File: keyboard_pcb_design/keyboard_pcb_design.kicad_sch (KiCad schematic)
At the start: 39 parts, among them J1 USB_C_Receptacle_USB2.0_14P, SW1 Switch, SW2 Switch, SW3 Switch, SW4 Switch, SW5 Switch, U1 SC09147, U2 NCP1117-3.3_SOT223, U3 MX25L3233FM2I-08Q, U4 SMF05CT1G, X1 ABM8-272-T3

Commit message: saved changes
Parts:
- removed J1: USB_C_Receptacle_USB2.0_14P, symbol Connector:USB_C_Receptacle_USB2.0_14P
- added J2: USB4105-GF-A, keyboard_footprint:USB4105_GCT, symbol keyboard_library:USB4105-GF-A
- U4: footprint (none) -> keyboard_footprint:SOT65P210X110-6N
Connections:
- net +5V is gone; now on net +3V3: C1.1, U2.3 (VI), U4.4
- net +3V3: now also J2.A4-B9 (VBUS), J2.B4-A9 (VBUS)
- net GND: now also J2.A1-B12 (GND), J2.B1-A12 (GND)
- net USB_D+: now also J2.A6 (DP1), J2.B6 (DP2)
- net USB_D-: now also J2.A7 (DN1), J2.B7 (DN2)
- net at R1.2: now also J2.A5 (CC1)
- net at R2.2: now also J2.B5 (CC2)
- no-connect marks 1 -> 3
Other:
- moved on the sheet: C1, C2, R1, R2, U2

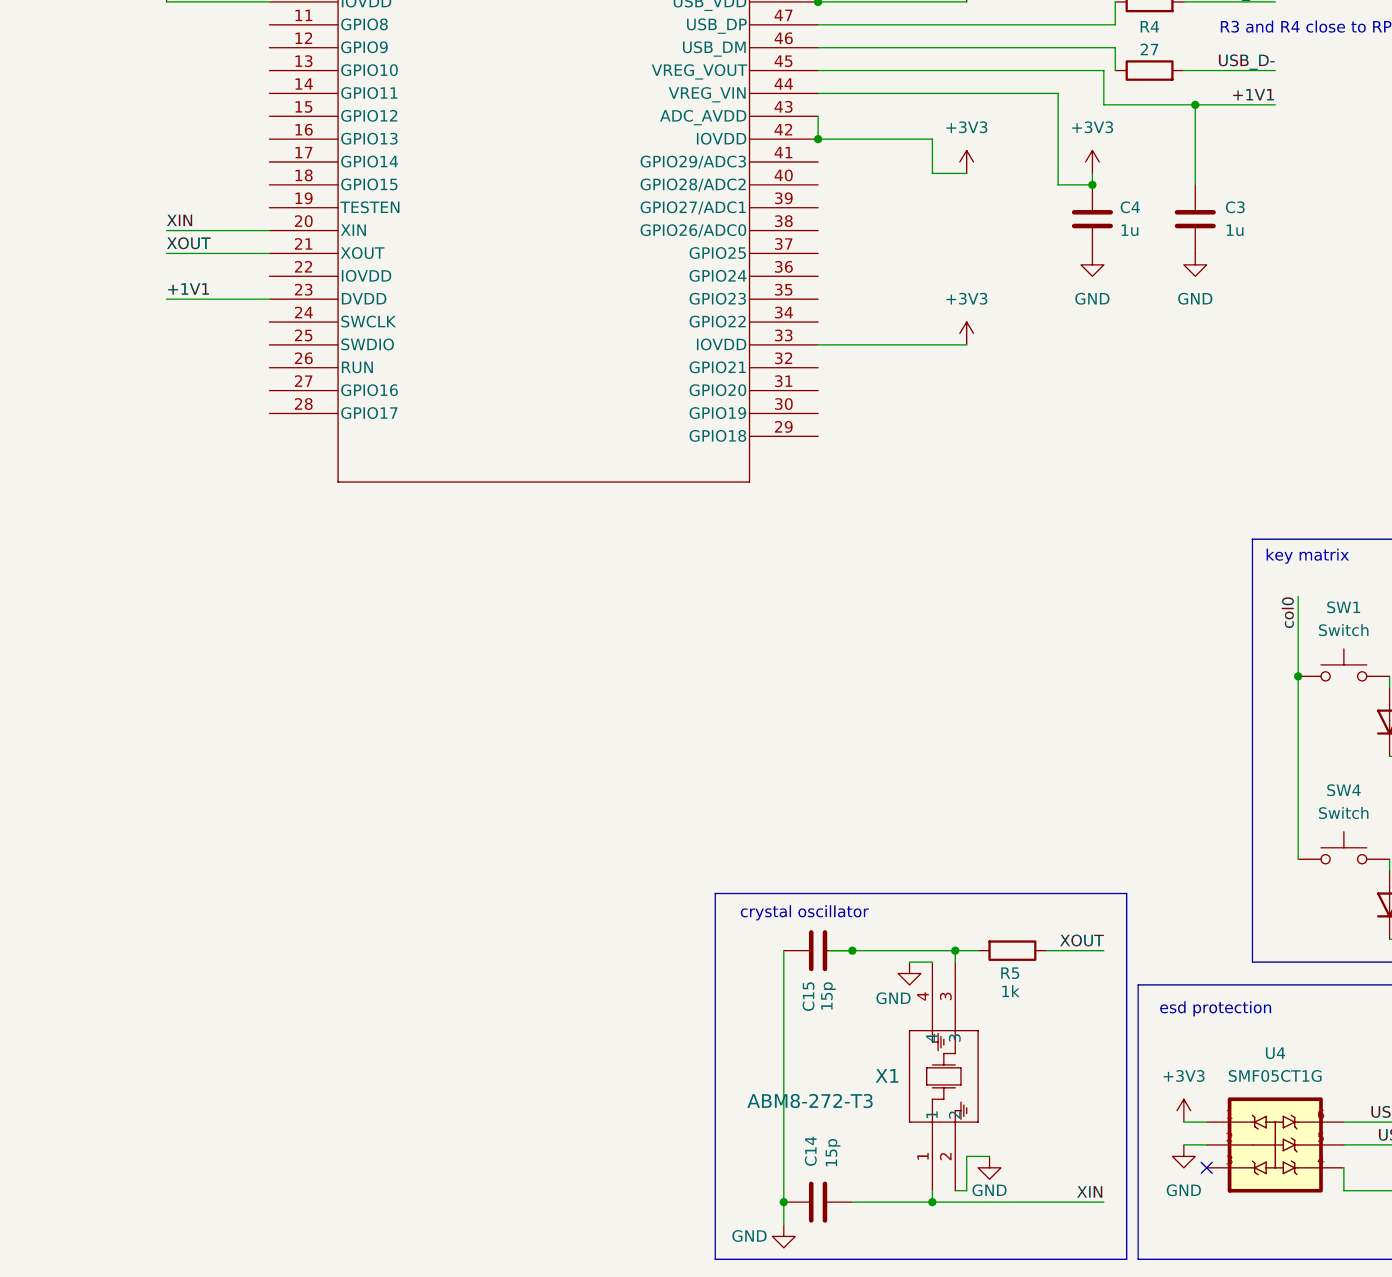
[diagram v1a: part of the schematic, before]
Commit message: update schematic for to usbc 16p and reset/boot buttons
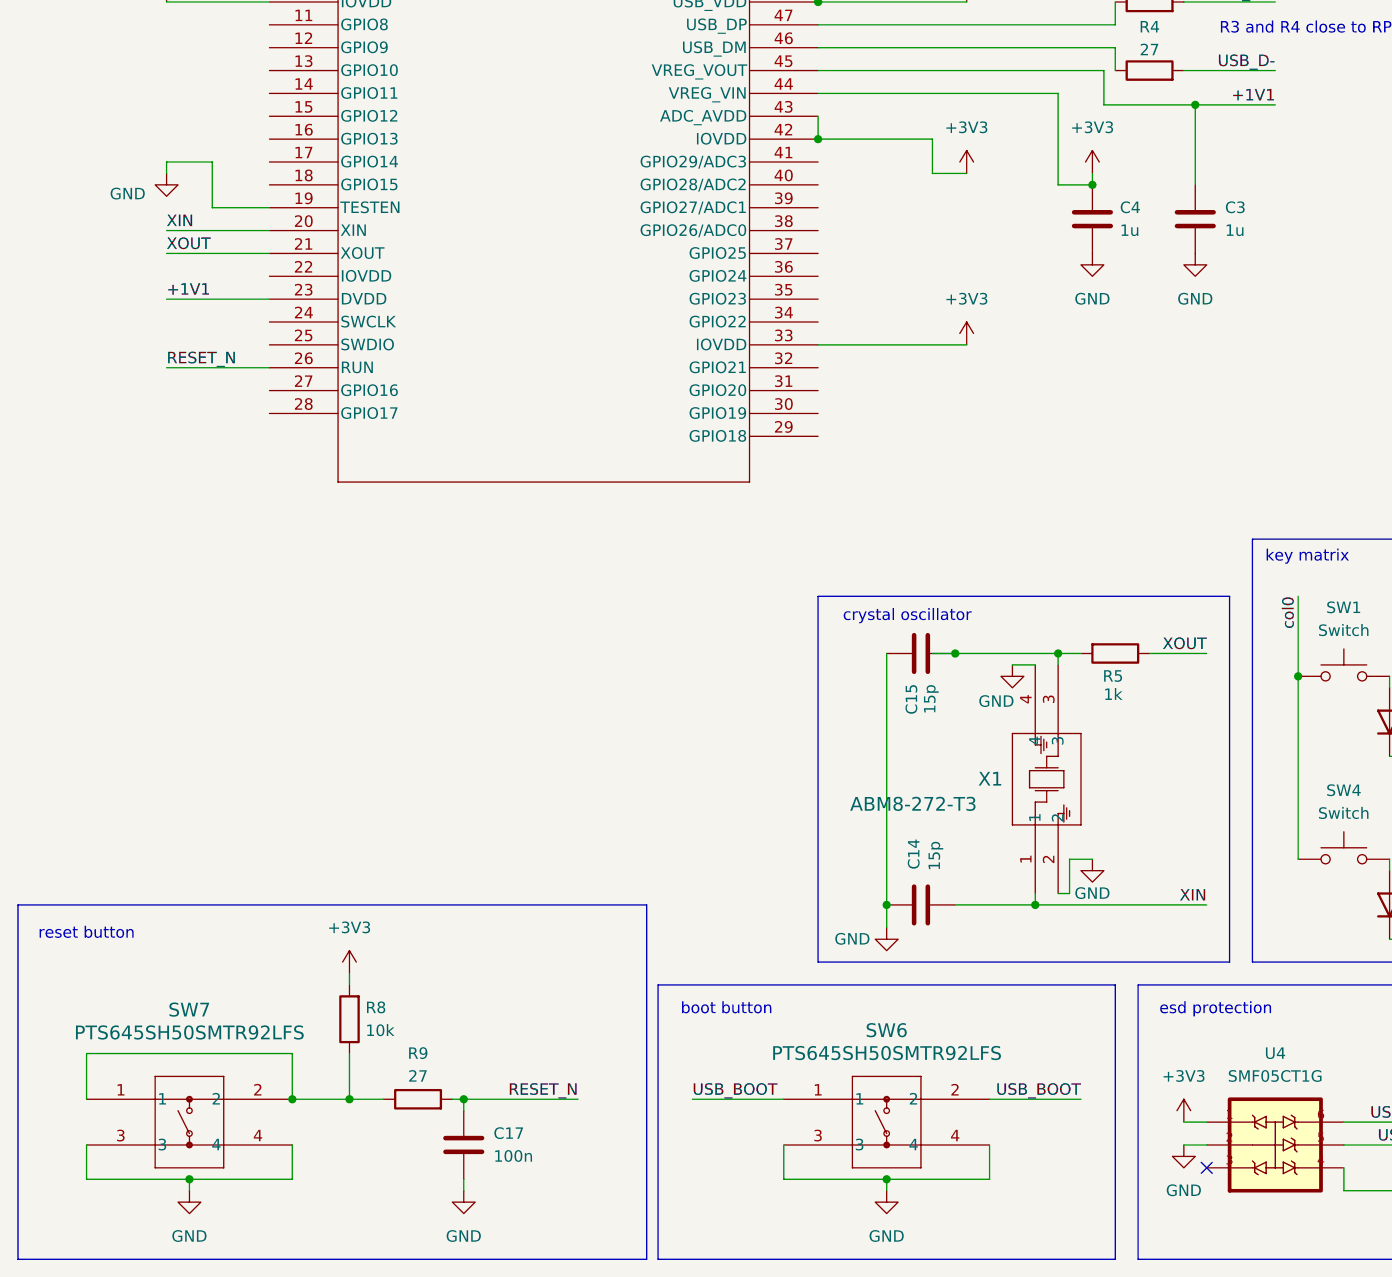
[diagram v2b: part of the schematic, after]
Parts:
- added C17: 100n, symbol Device:C
- added R8: 10k, symbol Device:R
- added R9: 27, symbol Device:R
- added SW6, SW7: PTS645SH50SMTR92LFS, symbol keyboard_library:PTS645SH50SMTR92LFS
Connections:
- net +3V3: now also R8.2
- net GND: now also U1.19 (TESTEN), C17.2, SW6.3, SW6.4, SW7.3, SW7.4
- net USB_BOOT: now also SW6.1, SW6.2
- net RESET_N: now reaches U1.26 (RUN)
- net RESET_N: now also C17.1, R9.2
- new net: R8.1, R9.1, SW7.1, SW7.2
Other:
- note added: "boot button"
- note added: "reset button"
- moved on the sheet: C14, C15, R5, X1

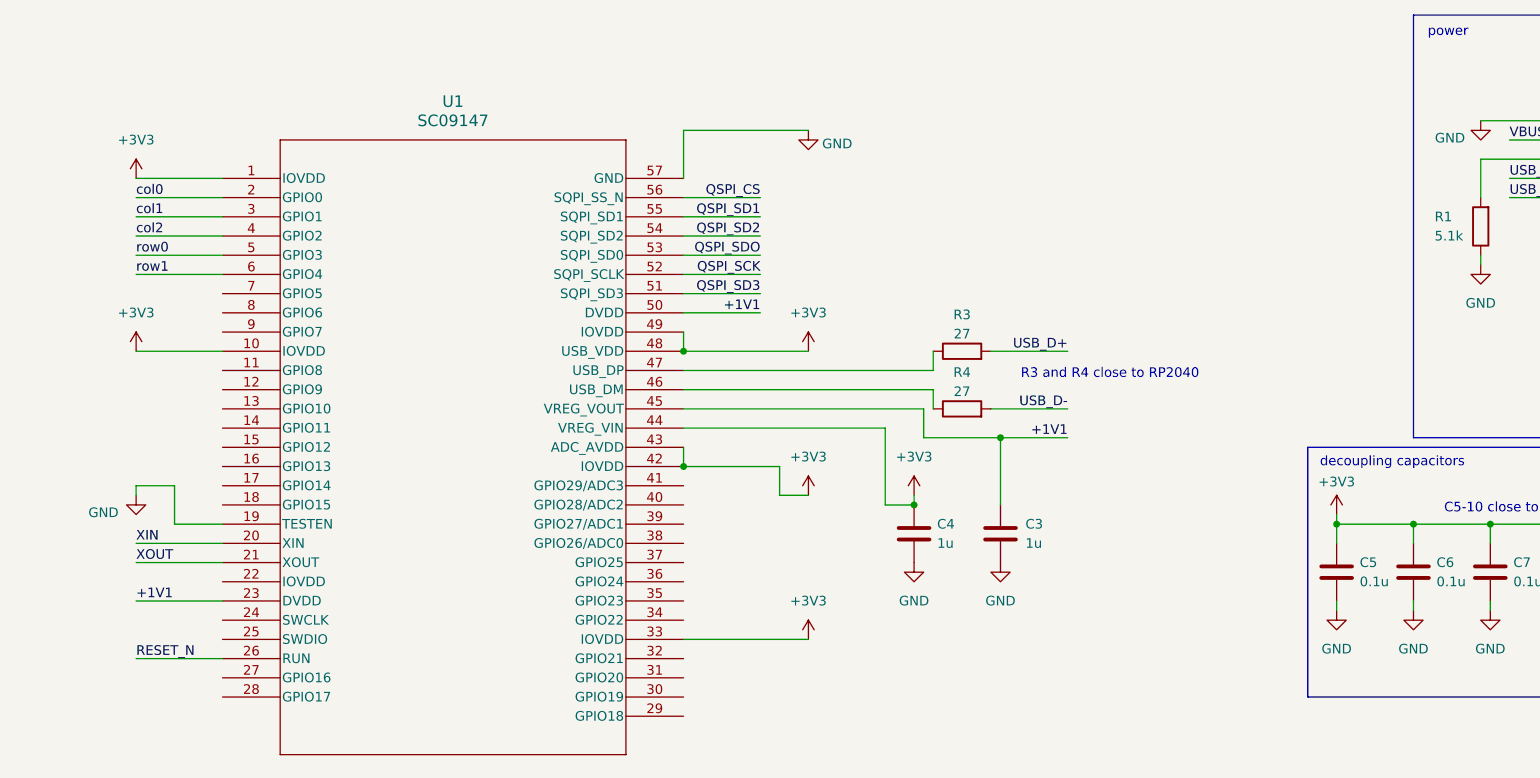
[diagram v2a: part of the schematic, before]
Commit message: debug conn schematic
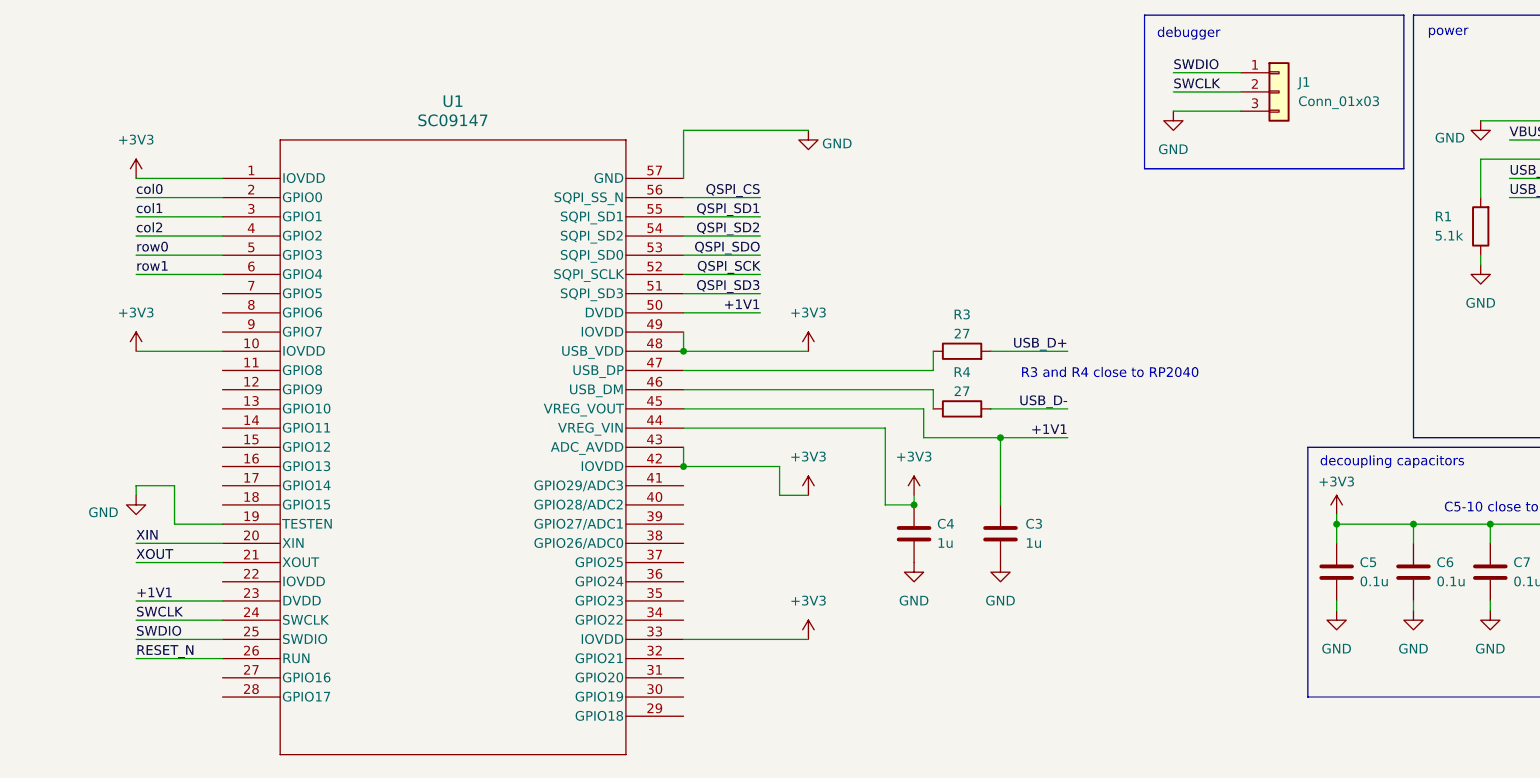
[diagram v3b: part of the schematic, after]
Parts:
- added J1: Conn_01x03, symbol Connector_Generic:Conn_01x03
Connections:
- net GND: now also J1.3 (Pin_3)
- net SWCLK: now reaches U1.24 (SWCLK)
- net SWCLK: now also J1.2 (Pin_2)
- net SWDIO: now reaches U1.25 (SWDIO)
- net SWDIO: now also J1.1 (Pin_1)
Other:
- note added: "debugger"
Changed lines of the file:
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@@
 	)
 	(rectangle
+		(start 163.83 12.7)
+		(end 198.12 33.02)
+		(stroke
+			(width 0)
+			(type default)
+		)
+		(fill
+			(type none)
+		)
+	)
+	(rectangle
 		(start 138.43 166.37)
 		(end 175.26 196.85)
@@
 		)
 	)
+	(text "debugger"
+		(exclude_from_sim no)
+		(at 169.672 15.24 0)
+		(effects
+			(font
+				(size 1.27 1.27)
+			)
+		)
+	)
 	(text "qspi flash"
 		(exclude_from_sim no)
@@
 	(wire
 		(pts
+			(xy 30.48 95.25) (xy 41.91 95.25)
+		)
+		(stroke
+			(width 0)
+			(type default)
+		)
+	)
+	(wire
+		(pts
 			(xy 135.89 62.23) (xy 135.89 64.77)
 		)
@@
 	(wire
 		(pts
+			(xy 30.48 92.71) (xy 41.91 92.71)
+		)
+		(stroke
+			(width 0)
+			(type default)
+		)
+	)
+	(wire
+		(pts
 			(xy 30.48 44.45) (xy 41.91 44.45)
 		)
@@
 	(wire
 		(pts
+			(xy 167.64 25.4) (xy 176.53 25.4)
+		)
+		(stroke
+			(width 0)
+			(type default)
+		)
+	)
+	(wire
+		(pts
 			(xy 102.87 64.77) (xy 134.62 64.77)
 		)
@@
 	(wire
 		(pts
+			(xy 167.64 22.86) (xy 176.53 22.86)
+		)
+		(stroke
+			(width 0)
+			(type default)
+		)
+	)
+	(wire
+		(pts
 			(xy 274.32 124.46) (xy 274.32 127)
 		)
@@
 	(wire
 		(pts
+			(xy 167.64 20.32) (xy 176.53 20.32)
+		)
+		(stroke
+			(width 0)
+			(type default)
+		)
+	)
+	(wire
+		(pts
 			(xy 110.49 129.54) (xy 110.49 157.48)
 		)
@@
 		)
 	)
+	(label "SWCLK"
+		(at 167.64 22.86 0)
+		(effects
+			(font
+				(size 1.27 1.27)
+			)
+			(justify left bottom)
+		)
+	)
 	(label "VBUS"
 		(at 218.44 54.61 0)
@@
 		)
 	)
+	(label "SWCLK"
+		(at 30.48 92.71 0)
+		(effects
+			(font
+				(size 1.27 1.27)
+			)
+			(justify left bottom)
+		)
+	)
 	(label "QSPI_SDO"
 		(at 219.71 139.7 0)
@@
 		)
 	)
+	(label "SWDIO"
+		(at 167.64 20.32 0)
+		(effects
+			(font
+				(size 1.27 1.27)
+			)
+			(justify left bottom)
+		)
+	)
 	(label "VBUS"
 		(at 212.09 29.21 0)
@@
 		)
 	)
+	(label "SWDIO"
+		(at 30.48 95.25 0)
+		(effects
+			(font
+				(size 1.27 1.27)
+			)
+			(justify left bottom)
+		)
+	)
 	(label "USB_D+"
 		(at 271.78 31.75 180)
@@
 	(symbol
 		(lib_id "power:GND")
+		(at 167.64 25.4 0)
+		(unit 1)
+		(exclude_from_sim no)
+		(in_bom yes)
+		(on_board yes)
+		(dnp no)
+		(fields_autoplaced yes)
+		(property "Reference" "#PWR045"
+			(at 167.64 31.75 0)
+			(effects
+				(font
+					(size 1.27 1.27)
+				)
+				(hide yes)
+			)
+		)
+		(property "Value" "GND"
+			(at 167.64 30.48 0)
+			(effects
+				(font
+					(size 1.27 1.27)
+				)
+			)
+		)
+		(property "Footprint" ""
+			(at 167.64 25.4 0)
+			(effects
+				(font
+					(size 1.27 1.27)
+				)
+				(hide yes)
+			)
+		)
+		(property "Datasheet" ""
+			(at 167.64 25.4 0)
+			(effects
+				(font
+					(size 1.27 1.27)
+				)
+				(hide yes)
+			)
+		)
+		(property "Description" "Power symbol creates a global label with name \"GND\" , ground"
+			(at 167.64 25.4 0)
+			(effects
+				(font
+					(size 1.27 1.27)
+				)
+				(hide yes)
+			)
+		)
+		(pin "1"
+		)
+		(instances
+			(project ""
+				(path "/f9810ab7-9213-4203-bfa9-6536d5a4d26a"
+					(reference "#PWR045")
+					(unit 1)
+				)
+			)
+		)
+	)
+	(symbol
+		(lib_id "power:GND")
 		(at 227.33 62.23 0)
 		(unit 1)
@@
 					(unit 1)
 				)
+			)
+		)
+	)
+	(symbol
+		(lib_id "Connector_Generic:Conn_01x03")
+		(at 181.61 22.86 0)
+		(unit 1)
+		(exclude_from_sim no)
+		(in_bom yes)
+		(on_board yes)
+		(dnp no)
+		(fields_autoplaced yes)
+		(property "Reference" "J1"
+			(at 184.15 21.5899 0)
+			(effects
+				(font
+					(size 1.27 1.27)
+				)
+				(justify left)
+			)
+		)
+		(property "Value" "Conn_01x03"
+			(at 184.15 24.1299 0)
+			(effects
+				(font
+					(size 1.27 1.27)
+				)
+				(justify left)
+			)
+		)
+		(property "Footprint" ""
+			(at 181.61 22.86 0)
+			(effects
+				(font
+					(size 1.27 1.27)
+				)
+				(hide yes)
+			)
+		)
+		(property "Datasheet" "~"
+			(at 181.61 22.86 0)
+			(effects
+				(font
+					(size 1.27 1.27)
+				)
+				(hide yes)
+			)
+		)
+		(property "Description" "Generic connector, single row, 01x03, script generated (kicad-library-utils/schlib/autogen/connector/)"
+			(at 181.61 22.86 0)
+			(effects
+				(font
+					(size 1.27 1.27)
+				)
+				(hide yes)
+			)
+		)
+		(pin "1"
+		)
+		(pin "2"
+		)
+		(pin "3"
+		)
+		(instances
+			(project ""
+				(path "/f9810ab7-9213-4203-bfa9-6536d5a4d26a"
+					(reference "J1")
+					(unit 1)
+				)
